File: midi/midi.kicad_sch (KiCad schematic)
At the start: 50 parts, among them J1 Conn_01x02_Shielded, J2 SJ-43515TS-SMT-TR, M1 Si4412DY, U1 ESP32-S3-WROOM-1-n16, U2 LTC1624CS8_TRPBF, U3 MAX98357A, U4 MAX98357A, U5 CD74HC154M96

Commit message: can't get footprint import to work
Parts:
- R1, R2, R3: footprint (none) -> Resistor_SMD:R_0805_2012Metric
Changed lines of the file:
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@@
 			)
 		)
-		(property "Footprint" ""
+		(property "Footprint" "Resistor_SMD:R_0805_2012Metric"
 			(at 272.288 167.64 90)
 			(effects
@@
 			)
 		)
-		(property "Footprint" ""
+		(property "Footprint" "Resistor_SMD:R_0805_2012Metric"
 			(at 272.288 175.26 90)
 			(effects
@@
 			)
 		)
-		(property "Footprint" ""
+		(property "Footprint" "Resistor_SMD:R_0805_2012Metric"
 			(at 182.88 151.638 90)
 			(effects

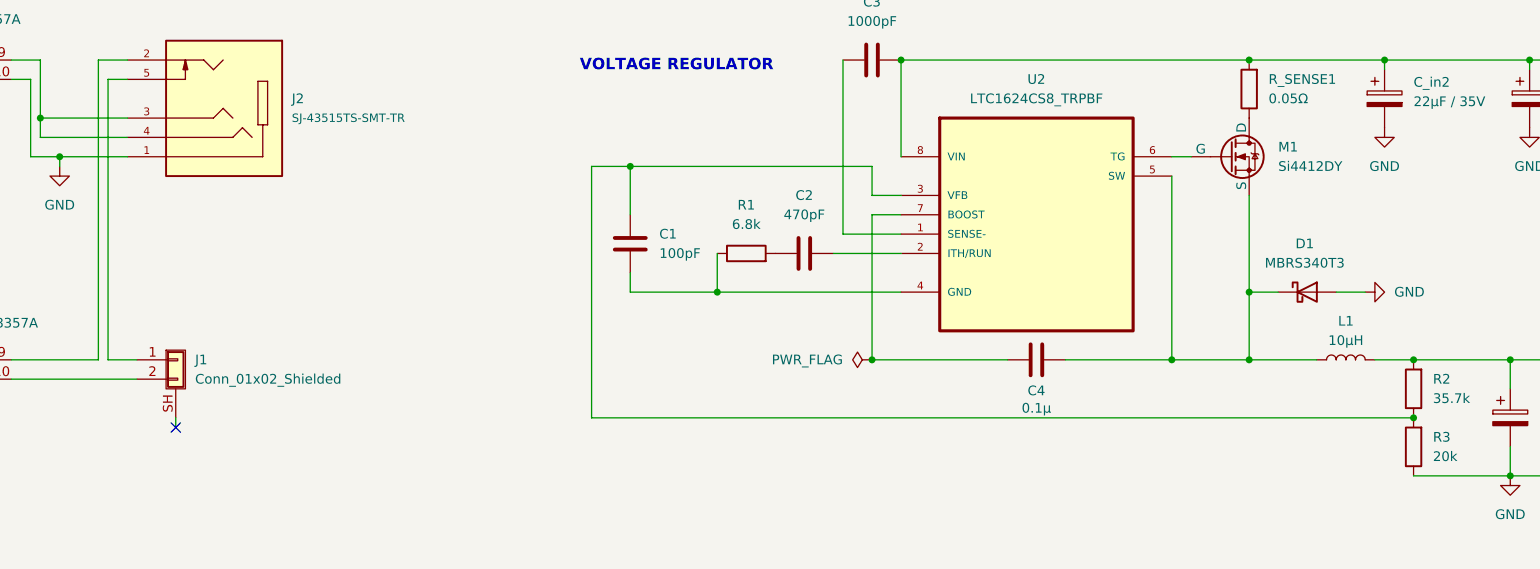
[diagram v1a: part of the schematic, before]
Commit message: unfuck footprint assignments / significant progress on layout
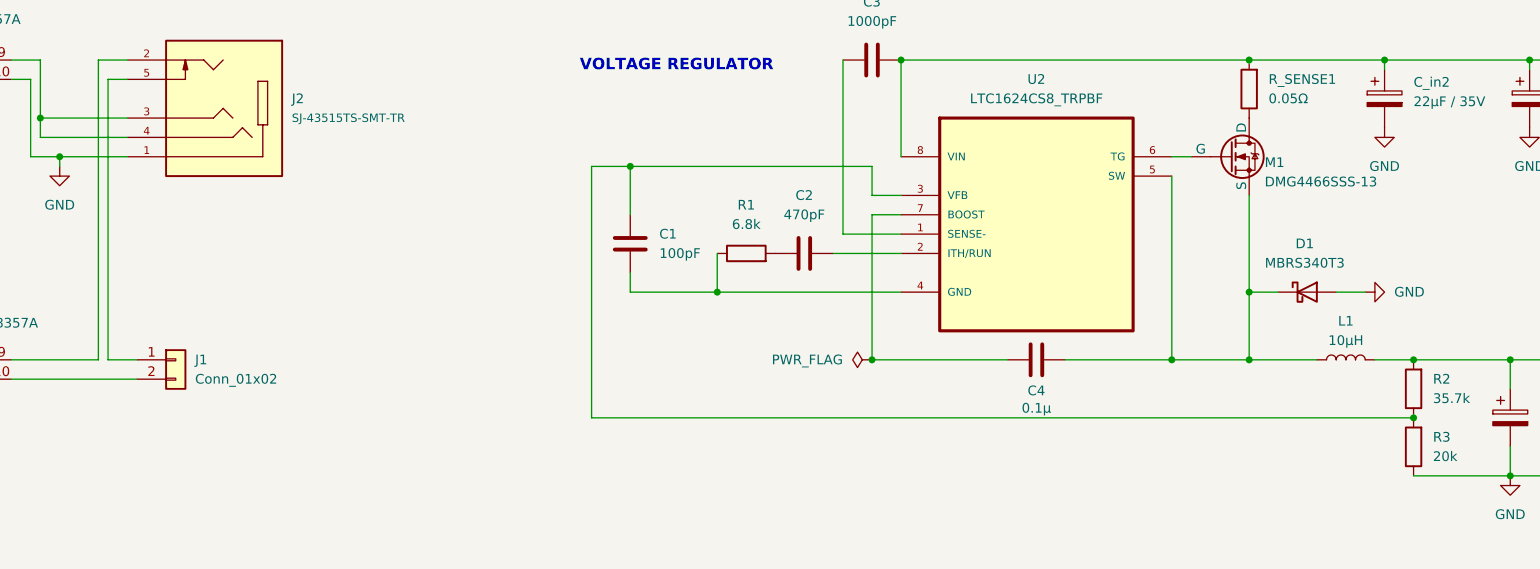
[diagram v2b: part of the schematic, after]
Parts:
- removed J1: Conn_01x02_Shielded, Connector_PinHeader_2.54mm:PinHeader_1x02_P2.54mm_Horizontal, symbol Connector_Generic_Shielded:Conn_01x02_Shielded
- added J1: Conn_01x02, Connector_PinHeader_2.54mm:PinHeader_1x02_P2.54mm_Vertical, symbol Connector_Generic:Conn_01x02
- J2: footprint SJ-43515TS-SMT-TR:CUI_SJ-43515TS-SMT-TR -> JACK-3.5mm_SJ_43515TS_SMT_TR:CUI_SJ-43515TS-SMT-TR
- L1: footprint (none) -> SRR6038_100Y:IND_BOURNS_SRR6038
- LCD1: footprint NHD-C12832A1Z-FSW-FBW-3V3:LCD_NHD-C12832A1Z-FSW-FBW-3V3 -> DISPLAY-NHD_C12832A1Z_FSW_FBW_3V3:LCD_NHD-C12832A1Z-FSW-FBW-3V3
- M1: value Si4412DY -> DMG4466SSS-13; footprint (none) -> DMG4466SSS_13:SO-8_DIO
- RV1, RV2: footprint (none) -> POT_PRS11R-415F-S103B1:POT_PRS11R-4-S_BRN
- R_SENSE1: footprint (none) -> Resistor_SMD:R_0805_2012Metric_Pad1.20x1.40mm_HandSolder
- S1, S10, S11, S12, S13, S14, S15, S16, S2, S3, S4, S5, S6, S7, S8, S9: footprint digikey-footprints:PushButton_Round_D12mm_THT_KS-01Q-01 -> BTN_TL3301AF160QJ:TL3301AF160QJ_EWI
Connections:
- net at J2.5: now also J1.1 (Pin_1)
- net at U4.10 (OUTN): now also J1.2 (Pin_2)
- no-connect marks 25 -> 24
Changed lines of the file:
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@@
 	)
 	(no_connect
-		(at 107.95 172.72)
-	)
-	(no_connect
 		(at 256.54 64.77)
 	)
@@
 	(wire
 		(pts
-			(xy 107.95 172.72) (xy 107.95 171.45)
-		)
-		(stroke
-			(width 0)
-			(type default)
-		)
-	)
-	(wire
-		(pts
 			(xy 215.9 52.07) (xy 219.71 52.07)
 		)
@@
 			)
 		)
-		(property "Footprint" ""
+		(property "Footprint" "Resistor_SMD:R_0805_2012Metric_Pad1.20x1.40mm_HandSolder"
 			(at 250.698 128.27 90)
 			(effects
@@
 			)
 		)
-		(property "Footprint" "digikey-footprints:PushButton_Round_D12mm_THT_KS-01Q-01"
+		(property "Footprint" "BTN_TL3301AF160QJ:TL3301AF160QJ_EWI"
 			(at 342.9 26.67 0)
 			(effects
@@
 			)
 		)
-		(property "Footprint" "digikey-footprints:PushButton_Round_D12mm_THT_KS-01Q-01"
+		(property "Footprint" "BTN_TL3301AF160QJ:TL3301AF160QJ_EWI"
 			(at 342.9 52.07 0)
 			(effects
@@
 			)
 		)
-		(property "Footprint" "digikey-footprints:PushButton_Round_D12mm_THT_KS-01Q-01"
+		(property "Footprint" "BTN_TL3301AF160QJ:TL3301AF160QJ_EWI"
 			(at 368.3 39.37 0)
 			(effects
@@
 			)
 		)
-		(property "Footprint" ""
+		(property "Footprint" "POT_PRS11R-415F-S103B1:POT_PRS11R-4-S_BRN"
 			(at 394.97 97.79 0)
 			(effects
@@
 			)
 		)
-		(property "Footprint" "digikey-footprints:PushButton_Round_D12mm_THT_KS-01Q-01"
+		(property "Footprint" "BTN_TL3301AF160QJ:TL3301AF160QJ_EWI"
 			(at 369.57 76.2 0)
 			(effects
@@
 			)
 		)
-		(property "Footprint" "digikey-footprints:PushButton_Round_D12mm_THT_KS-01Q-01"
+		(property "Footprint" "BTN_TL3301AF160QJ:TL3301AF160QJ_EWI"
 			(at 317.5 76.2 0)
 			(effects
@@
 			)
 		)
-		(property "Footprint" ""
+		(property "Footprint" "SRR6038_100Y:IND_BOURNS_SRR6038"
 			(at 261.62 163.83 0)
 			(effects
@@
 			)
 		)
-		(property "Footprint" "digikey-footprints:PushButton_Round_D12mm_THT_KS-01Q-01"
+		(property "Footprint" "BTN_TL3301AF160QJ:TL3301AF160QJ_EWI"
 			(at 342.9 95.25 0)
 			(effects
@@
 			)
 		)
-		(property "Footprint" "digikey-footprints:PushButton_Round_D12mm_THT_KS-01Q-01"
+		(property "Footprint" "BTN_TL3301AF160QJ:TL3301AF160QJ_EWI"
 			(at 368.3 26.67 0)
 			(effects
@@
 	)
 	(symbol
-		(lib_id "Connector_Generic_Shielded:Conn_01x02_Shielded")
-		(at 107.95 163.83 0)
-		(unit 1)
-		(exclude_from_sim no)
-		(in_bom yes)
-		(on_board yes)
-		(dnp no)
-		(fields_autoplaced yes)
-		(property "Reference" "J1"
-			(at 110.49 163.8299 0)
-			(effects
-				(font
-					(size 1.27 1.27)
-				)
-				(justify left)
-			)
-		)
-		(property "Value" "Conn_01x02_Shielded"
-			(at 110.49 166.3699 0)
-			(effects
-				(font
-					(size 1.27 1.27)
-				)
-				(justify left)
-			)
-		)
-		(property "Footprint" "Connector_PinHeader_2.54mm:PinHeader_1x02_P2.54mm_Horizontal"
-			(at 107.95 163.83 0)
-			(effects
-				(font
-					(size 1.27 1.27)
-				)
-				(hide yes)
-			)
-		)
-		(property "Datasheet" "~"
-			(at 107.95 163.83 0)
-			(effects
-				(font
-					(size 1.27 1.27)
-				)
-				(hide yes)
-			)
-		)
-		(property "Description" "Generic shielded connector, single row, 01x02, script generated (kicad-library-utils/schlib/autogen/connector/)"
-			(at 107.95 163.83 0)
-			(effects
-				(font
-					(size 1.27 1.27)
-				)
-				(hide yes)
-			)
-		)
-		(pin "2"
-		)
-		(pin "1"
-		)
-		(pin "SH"
-		)
-		(instances
-			(project ""
-				(path "/062cddda-4621-48ae-9feb-d7c8105a5a13"
-					(reference "J1")
-					(unit 1)
-				)
-			)
-		)
-	)
-	(symbol
 		(lib_id "Device:D_Schottky")
 		(at 256.54 154.94 0)
@@
 			)
 		)
-		(property "Footprint" "digikey-footprints:PushButton_Round_D12mm_THT_KS-01Q-01"
+		(property "Footprint" "BTN_TL3301AF160QJ:TL3301AF160QJ_EWI"
 			(at 393.7 39.37 0)
 			(effects
@@
 			)
 		)
-		(property "Footprint" "digikey-footprints:PushButton_Round_D12mm_THT_KS-01Q-01"
+		(property "Footprint" "BTN_TL3301AF160QJ:TL3301AF160QJ_EWI"
 			(at 317.5 39.37 0)
 			(effects
@@
 			)
 		)
-		(property "Footprint" "NHD-C12832A1Z-FSW-FBW-3V3:LCD_NHD-C12832A1Z-FSW-FBW-3V3"
+		(property "Footprint" "DISPLAY-NHD_C12832A1Z_FSW_FBW_3V3:LCD_NHD-C12832A1Z-FSW-FBW-3V3"
 			(at 182.88 59.69 0)
 			(effects
@@
 			)
 		)
-		(property "Footprint" "digikey-footprints:PushButton_Round_D12mm_THT_KS-01Q-01"
+		(property "Footprint" "BTN_TL3301AF160QJ:TL3301AF160QJ_EWI"
 			(at 317.5 95.25 0)
 			(effects
@@
 			)
 		)
-		(property "Footprint" "digikey-footprints:PushButton_Round_D12mm_THT_KS-01Q-01"
+		(property "Footprint" "BTN_TL3301AF160QJ:TL3301AF160QJ_EWI"
 			(at 394.97 76.2 0)
 			(effects
@@
 	)
 	(symbol
+		(lib_id "Connector_Generic:Conn_01x02")
+		(at 107.95 163.83 0)
+		(unit 1)
+		(exclude_from_sim no)
+		(in_bom yes)
+		(on_board yes)
+		(dnp no)
+		(fields_autoplaced yes)
+		(property "Reference" "J1"
+			(at 110.49 163.8299 0)
+			(effects
+				(font
+					(size 1.27 1.27)
+				)
+				(justify left)
+			)
+		)
+		(property "Value" "Conn_01x02"
+			(at 110.49 166.3699 0)
+			(effects
+				(font
+					(size 1.27 1.27)
+				)
+				(justify left)
+			)
+		)
+		(property "Footprint" "Connector_PinHeader_2.54mm:PinHeader_1x02_P2.54mm_Vertical"
+			(at 107.95 163.83 0)
+			(effects
+				(font
+					(size 1.27 1.27)
+				)
+				(hide yes)
+			)
+		)
+		(property "Datasheet" "~"
+			(at 107.95 163.83 0)
+			(effects
+				(font
+					(size 1.27 1.27)
+				)
+				(hide yes)
+			)
+		)
+		(property "Description" "Generic connector, single row, 01x02, script generated (kicad-library-utils/schlib/autogen/connector/)"
+			(at 107.95 163.83 0)
+			(effects
+				(font
+					(size 1.27 1.27)
+				)
+				(hide yes)
+			)
+		)
+		(pin "2"
+		)
+		(pin "1"
+		)
+		(instances
+			(project ""
+				(path "/062cddda-4621-48ae-9feb-d7c8105a5a13"
+					(reference "J1")
+					(unit 1)
+				)
+			)
+		)
+	)
+	(symbol
 		(lib_id "power:GND")
 		(at 342.9 57.15 90)
@@
 			)
 		)
-		(property "Footprint" "SJ-43515TS-SMT-TR:CUI_SJ-43515TS-SMT-TR"
+		(property "Footprint" "JACK-3.5mm_SJ_43515TS_SMT_TR:CUI_SJ-43515TS-SMT-TR"
 			(at 113.538 116.332 0)
 			(effects
@@
 		(on_board yes)
 		(dnp no)
-		(fields_autoplaced yes)
 		(property "Reference" "M1"
-			(at 252.73 135.8899 0)
+			(at 250.952 137.922 0)
 			(effects
 				(font
@@
 			)
 		)
-		(property "Value" "Si4412DY"
-			(at 252.73 138.4299 0)
+		(property "Value" "DMG4466SSS-13"
+			(at 250.952 140.462 0)
 			(effects
 				(font
@@
 			)
 		)
-		(property "Footprint" ""
+		(property "Footprint" "DMG4466SSS_13:SO-8_DIO"
 			(at 251.46 134.62 0)
 			(effects
@@
 			)
 		)
-		(property "Footprint" "digikey-footprints:PushButton_Round_D12mm_THT_KS-01Q-01"
+		(property "Footprint" "BTN_TL3301AF160QJ:TL3301AF160QJ_EWI"
 			(at 317.5 26.67 0)
 			(effects
@@
 			)
 		)
-		(property "Footprint" "digikey-footprints:PushButton_Round_D12mm_THT_KS-01Q-01"
+		(property "Footprint" "BTN_TL3301AF160QJ:TL3301AF160QJ_EWI"
 			(at 317.5 52.07 0)
 			(effects
@@
 			)
 		)
-		(property "Footprint" "digikey-footprints:PushButton_Round_D12mm_THT_KS-01Q-01"
+		(property "Footprint" "BTN_TL3301AF160QJ:TL3301AF160QJ_EWI"
 			(at 342.9 76.2 0)
 			(effects
@@
 			)
 		)
-		(property "Footprint" ""
+		(property "Footprint" "POT_PRS11R-415F-S103B1:POT_PRS11R-4-S_BRN"
 			(at 370.84 97.79 0)
 			(effects
@@
 			)
 		)
-		(property "Footprint" "digikey-footprints:PushButton_Round_D12mm_THT_KS-01Q-01"
+		(property "Footprint" "BTN_TL3301AF160QJ:TL3301AF160QJ_EWI"
 			(at 342.9 39.37 0)
 			(effects
@@
 			)
 		)
-		(property "Footprint" "digikey-footprints:PushButton_Round_D12mm_THT_KS-01Q-01"
+		(property "Footprint" "BTN_TL3301AF160QJ:TL3301AF160QJ_EWI"
 			(at 393.7 26.67 0)
 			(effects

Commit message: switch esp32 from s3 to s2 / use esplib, use USBC data connector, other tweaks
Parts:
- removed U1: ESP32-S3-WROOM-1-n16, RF_Module:ESP32-S3-WROOM-1, symbol RF_Module:ESP32-S3-WROOM-1
- removed USB1: USB4125-GF-A, USB4125_GF_A:CONN6_USB4125_GCT, symbol USB4125_GF_A:USB4125-GF-A
- added J3: USB_C_Receptacle_USB2.0_16P, symbol Connector:USB_C_Receptacle_USB2.0_16P
- added R4, R5: R, symbol Device:R
- added U6: ESP32-S2-SOLO, PCM_Espressif:ESP32-S2-SOLO, symbol PCM_Espressif:ESP32-S2-SOLO
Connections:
- net 3V3: no longer C_out1.1, C_out2.1, L1.2, LCD1.12 (VDD), R2.2, U3.7 (VDD), U3.8 (VDD), U4.7 (VDD), U4.8 (VDD), U5.24 (VCC)
- net AUDIO.BCLK: now also U6.11 (GPIO18/U1RXD/ADC2_CH7/DAC_2/CLK_OUT3)
- net AUDIO.DIN: now also U6.15 (GPIO3/TOUCH3/ADC1_CH2)
- net AUDIO.LRCLK: now also U6.4 (GPIO4/TOUCH4/ADC1_CH3)
- net BTND0: now also U6.32 (MTCK/GPIO39/CLK_OUT3)
- net BTND1: now also U6.33 (MTDO/GPIO40/CLK_OUT2)
- net BTND2: now also U6.34 (MTDI/GPIO41/CLK_OUT1)
- net BTND3: now also U6.35 (MTMS/GPIO42)
- net EN-ESP32: now also U6.3 (EN)
- net GND: now also J3.A1 (GND), J3.A12 (GND), J3.B1 (GND), J3.B12 (GND), R4.2, R5.2, U6.1 (GND), U6.40 (GND), U6.41 (GND)
- net LCD.A0: now also U6.26 (GPIO45); no longer LCD1.15 (A0)
- net LCD.CS1: now also U6.25 (SPIIO5/GPIO34/FSPICS0)
- net LCD.RST: now also U6.23 (GPIO21)
- net LCD.SCL: now also U6.29 (SPIIO7/GPIO36/FSPICLK)
- net LCD.SI: now also U6.28 (SPIIO6/GPIO35/FSPID)
- net RV1: now also U6.39 (GPIO1/TOUCH1/ADC1_CH0)
- net RV2: now also U6.38 (GPIO2/TOUCH2/ADC1_CH1)
- net 5V renamed +5V
- net +5V: now also J3.A4 (VBUS), J3.A9 (VBUS), J3.B4 (VBUS), J3.B9 (VBUS)
- new net: J3.A5 (CC1), R4.1
- new net: J3.B5 (CC2), R5.1
- new net +3V3: C_out1.1, C_out2.1, L1.2, LCD1.12 (VDD), R2.2, U3.7 (VDD), U3.8 (VDD), U4.7 (VDD), U4.8 (VDD), U5.24 (VCC), U6.2 (3V3)
- new net USB.D+: J3.A6 (D+), J3.B6 (D+), U6.14 (GPIO20/U1CTS/ADC2_CH9/CLK_OUT1/USB_D+)
- new net USB.D-: J3.A7 (D-), J3.B7 (D-), U6.13 (GPIO19/U1RTS/ADC2_CH8/CLK_OUT2/USB_D-)
- no-connect marks 24 -> 28
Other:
- note added: "CONTROL BUTTONS, BUTTON INPUT MUX, POTS"
- note removed: "CONTROL BUTTONS BUTTON INPUT MUX POTS"
- moved on the sheet: C1, C10, C11, C12, C2, C3, C4, C5, C6, C7, C8, C9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

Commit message: wip: switch from LTC1624 to other vreg
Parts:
- removed C1: 100pF, Capacitor_SMD:C_1210_3225Metric, symbol Device:C
- removed C2: 470pF, Capacitor_SMD:C_1812_4532Metric, symbol Device:C
- removed C3: 1000pF, Capacitor_SMD:C_0805_2012Metric, symbol Device:C
- removed C4: 0.1µ, Capacitor_SMD:C_1210_3225Metric, symbol Device:C
- removed C_in1, C_in2: 22µF / 35V, Capacitor_SMD:C_2220_5750Metric, symbol Device:C_Polarized
- removed C_out1, C_out2: 100µF / 10V, Capacitor_THT:CP_Radial_D6.3mm_P2.50mm, symbol Device:C_Polarized
- removed D1: MBRS340T3, Diode_SMD:D_SMA, symbol Device:D_Schottky
- removed L1: 10µH, SRR6038_100Y:IND_BOURNS_SRR6038, symbol Device:L
- removed M1: DMG4466SSS-13, DMG4466SSS_13:SO-8_DIO, symbol Simulation_SPICE:NMOS
- removed R1: 6.8k, Resistor_SMD:R_0805_2012Metric, symbol Device:R
- removed R2: 35.7k, Resistor_SMD:R_0805_2012Metric, symbol Device:R
- removed R3: 20k, Resistor_SMD:R_0805_2012Metric, symbol Device:R
- removed R_SENSE1: 0.05Ω, Resistor_SMD:R_0805_2012Metric_Pad1.20x1.40mm_HandSolder, symbol Device:R
- removed U2: LTC1624CS8_TRPBF, LTC1624CS8_TRPBF:SOIC127P600X175-8N, symbol LTC1624CS8_TRPBF:LTC1624CS8_TRPBF
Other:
- note removed: "VOLTAGE REGULATOR"
- moved on the sheet: C10, C11, C12, C5, C6, C7, C8, C9, J1, J2, J3, LCD1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
